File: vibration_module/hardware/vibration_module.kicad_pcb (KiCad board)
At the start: 2 copper layers, 19.8 x 18 mm, 17 parts, among them J1 I2C/PWR, SW2 SW_SPST, U2 DRV2605LDGS, U3 STM32G031G8Ux, U4 TPS7A20xxxDQN

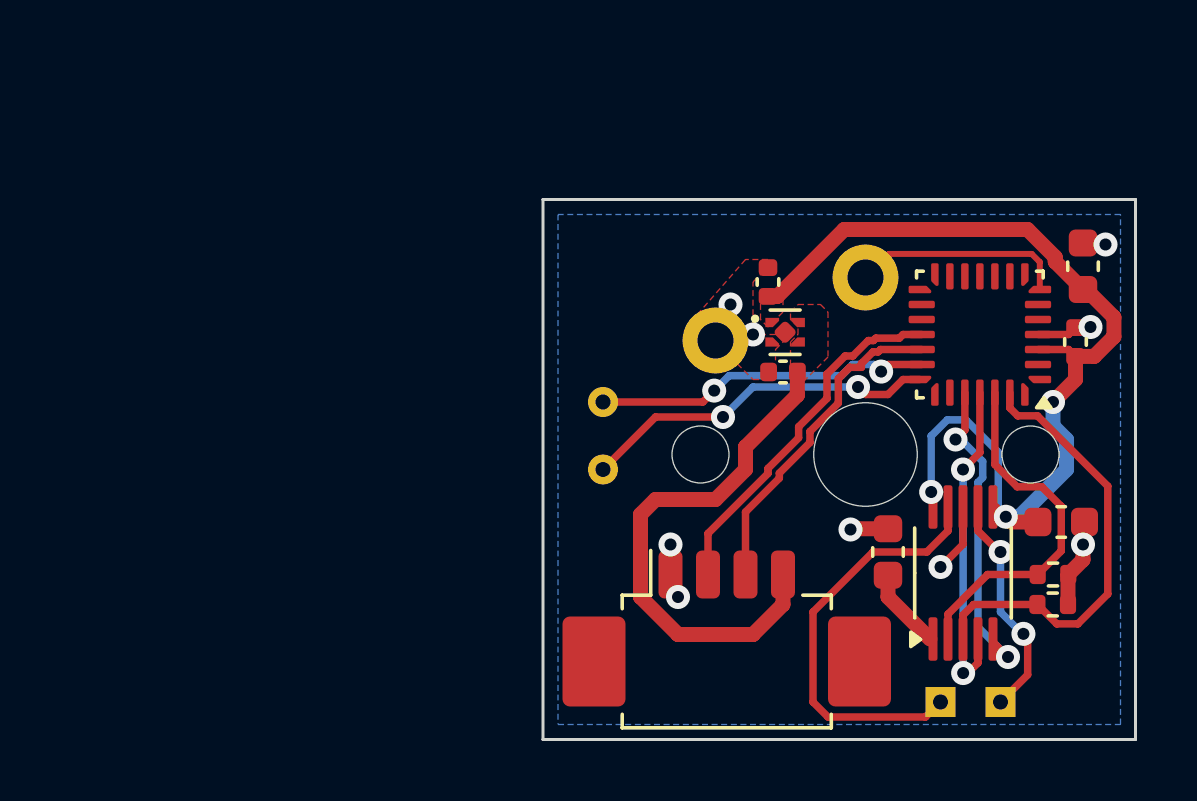
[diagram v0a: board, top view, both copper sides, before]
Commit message: update pcb layout, change switch bom
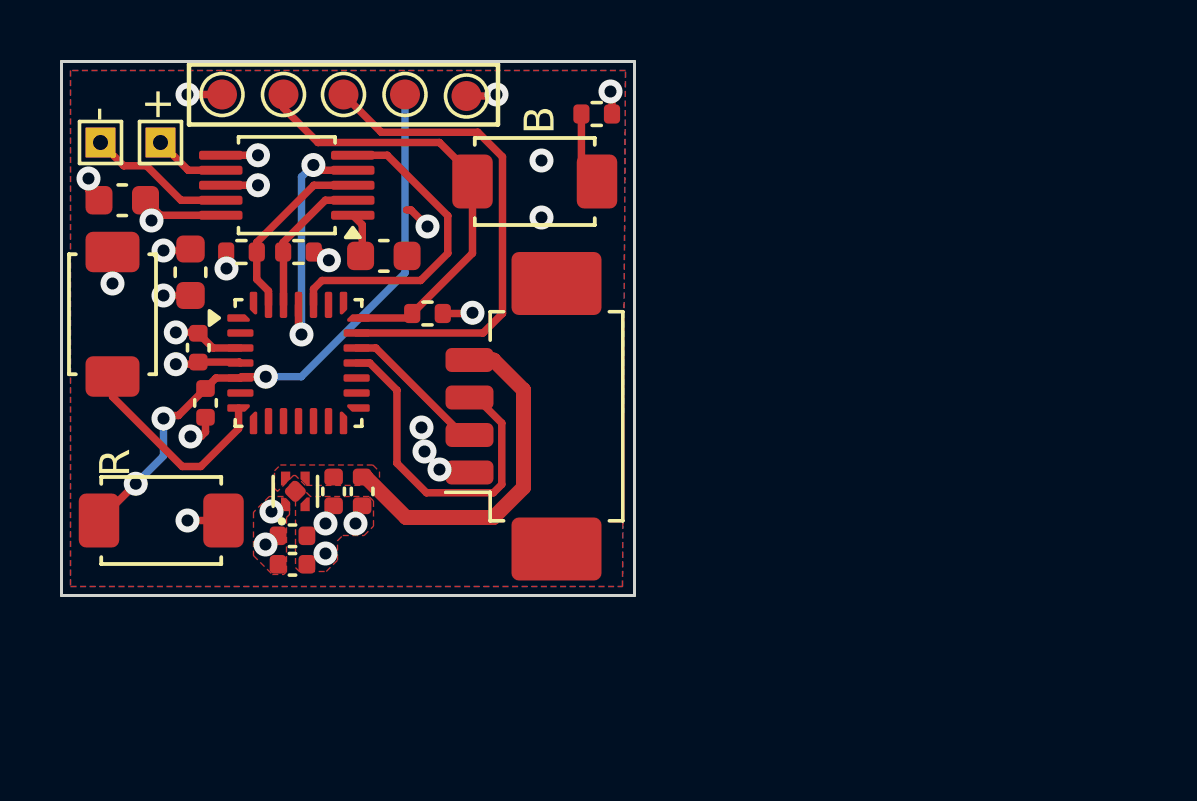
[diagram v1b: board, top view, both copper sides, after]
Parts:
- removed U4: TPS7A20xxxDQN, Package_SON:Texas_X2SON-4_1x1mm_P0.65mm
- added C3: 100n, Capacitor_SMD:C_0402_1005Metric, F.Cu at (162.3, 69.4)
- added C4: 100n, Capacitor_SMD:C_0402_1005Metric, F.Cu at (166.8, 74.2)
- added C5: 1u, Capacitor_SMD:C_0402_1005Metric, F.Cu at (167.7, 74.2)
- added R1: 330Ω, Resistor_SMD:R_0402_1005Metric, F.Cu at (175.5, 61.6)
- added R2: 10k, Resistor_SMD:R_0402_1005Metric, F.Cu at (169.9, 68.3)
- added SW1: NRST, PCM_JLCPCB:SW_TS-1088-AR02016, F.Cu at (161.0, 75.2)
- added SW3: SW_SPST, PCM_JLCPCB:SW_TS-1088-AR02016, F.Cu at (159.4, 68.3)
- added TP5: SWCLK, TestPoint:TestPoint_Pad_D1.0mm, F.Cu at (165.1, 61.0)
- added TP6: NRST, TestPoint:TestPoint_Pad_D1.0mm, F.Cu at (169.2, 61.0)
- added TP7: GND, TestPoint:TestPoint_Pad_D1.0mm, F.Cu at (171.2, 61.0)
- added U1: TPS7A20xxxDQN, Package_SON:Texas_X2SON-4_1x1mm_P0.65mm, F.Cu at (165.5, 74.2)
- C1: value 1u -> 100n; footprint Capacitor_SMD:C_0603_1608Metric -> Capacitor_SMD:C_0402_1005Metric
- C2: value 1u -> 10u
- C6: value 100n -> 1u
- C7: value 10u -> 100n; footprint Capacitor_SMD:C_0603_1608Metric -> Capacitor_SMD:C_0402_1005Metric
- C8, C9: footprint Capacitor_SMD:C_0402_1005Metric -> Capacitor_SMD:C_0603_1608Metric
- SW2: value SW_SPST -> BOOT0; footprint PCM_Switch_Keyboard_Kailh:SW_Kailh_Choc_V1_1.00u -> PCM_JLCPCB:SW_TS-1088-AR02016; moved to F.Cu
- TP1: value SWCLK -> M+; footprint TestPoint:TestPoint_THTPad_D1.0mm_Drill0.5mm -> TestPoint:TestPoint_THTPad_1.0x1.0mm_Drill0.5mm
- TP2: value SWDIO -> M-; footprint TestPoint:TestPoint_THTPad_D1.0mm_Drill0.5mm -> TestPoint:TestPoint_THTPad_1.0x1.0mm_Drill0.5mm
- TP3: value M+ -> 3V3; footprint TestPoint:TestPoint_THTPad_1.0x1.0mm_Drill0.5mm -> TestPoint:TestPoint_Pad_D1.0mm
- TP4: value M- -> SWDIO; footprint TestPoint:TestPoint_THTPad_1.0x1.0mm_Drill0.5mm -> TestPoint:TestPoint_Pad_D1.0mm
- U2: value DRV2605LDGS -> STM32G031G8Ux; footprint Package_SO:VSSOP-10_3x3mm_P0.5mm -> Package_DFN_QFN:QFN-28_4x4mm_P0.5mm
- U3: value STM32G031G8Ux -> DRV2605LDGS; footprint Package_DFN_QFN:QFN-28_4x4mm_P0.5mm -> Package_SO:VSSOP-10_3x3mm_P0.5mm
- moved TP3 31.4 mm to (163.1, 61.0)
- moved C2 30.2 mm to (162.0, 66.9), turned to 90 degrees
- moved TP4 29.8 mm to (167.1, 61.0)
- moved R3 29.5 mm to (163.7, 66.3), turned to 180 degrees
- moved C7 27.8 mm to (165.4, 75.7), turned to 180 degrees
- moved R4 27.4 mm to (165.6, 66.3)
- moved C6 27.1 mm to (165.4, 76.7), turned to 180 degrees
- moved U3 23.6 mm to (165.2, 64.0)
- moved C1 23.3 mm to (162.5, 71.3), turned to 90 degrees
- moved U2 23.2 mm to (165.6, 70.0), turned to 0 degrees
- moved C8 22.8 mm to (159.7, 64.5)
- moved TP2 18.9 mm to (159.0, 62.6), turned to 180 degrees
- moved TP1 18.3 mm to (161.0, 62.6), turned to 180 degrees
- moved SW2 14.3 mm to (173.5, 63.9), turned to 0 degrees
- moved C9 12.8 mm to (168.4, 66.4), turned to 180 degrees
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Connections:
- C1 pad 2: Net-(U2-REG) -> NRST
- C6 pad 1: +3.3V -> GND
- C6 pad 2: GND -> +3.3V
- C7 pad 1: +3.3V -> GND
- C7 pad 2: GND -> +3.3V
- C8 pad 1: VBUS -> +3.3V
- C9 pad 1: +3.3V -> GND
- C9 pad 2: GND -> Net-(U3-REG)
- J1 pad 2: /SCL -> I2C2_SDA
- J1 pad 3: /SDA -> I2C2_SCL
- R3 pad 1: Net-(U2-SDA) -> I2C1_SDA
- R3 pad 2: GND -> +3.3V
- R4 pad 1: Net-(U2-SCL) -> I2C1_SCL
- R4 pad 2: GND -> +3.3V
- SW2 pad 1: Net-(SW2-A) -> SWCLK/BOOT0
- SW2 pad 2: GND -> Net-(SW2-B)
- TP1 pad 1: Net-(U3-PA14) -> Net-(U3-OUT+)
- TP2 pad 1: Net-(U3-PA13) -> Net-(U3-OUT-)
- TP3 pad 1: Net-(U2-OUT-) -> +3.3V
- TP4 pad 1: Net-(U2-OUT+) -> SWDIO
- U2 pad 1: Net-(U2-REG) -> unconnected-(U2-PC14-Pad1)
- U2 pad 10: +3.3V -> unconnected-(U2-PA4-Pad10)
- U2 pad 2: Net-(U2-SCL) -> unconnected-(U2-PC15-Pad2)
- U2 pad 3: Net-(U2-SDA) -> +3.3V
- U2 pad 4: Net-(U2-IN/TRIG) -> GND
- U2 pad 5: Net-(U2-EN) -> NRST
- U2 pad 6: +3.3V -> unconnected-(U2-PA0-Pad6)
- U2 pad 7: Net-(U2-OUT+) -> SW
- U2 pad 8: GND -> unconnected-(U2-PA2-Pad8)
- U2 pad 9: Net-(U2-OUT-) -> unconnected-(U2-PA3-Pad9)
- U3 pad 1: unconnected-(U3-PC14-Pad1) -> Net-(U3-REG)
- U3 pad 10: unconnected-(U3-PA4-Pad10) -> +3.3V
- U3 pad 2: unconnected-(U3-PC15-Pad2) -> I2C1_SCL
- U3 pad 3: +3.3V -> I2C1_SDA
- U3 pad 4: GND -> IN/TRIG
- U3 pad 5: unconnected-(U3-PF2-Pad5) -> EN
- U3 pad 6: unconnected-(U3-PA0-Pad6) -> +3.3V
- U3 pad 7: Net-(SW2-A) -> Net-(U3-OUT+)
- U3 pad 8: unconnected-(U3-PA2-Pad8) -> GND
- U3 pad 9: unconnected-(U3-PA3-Pad9) -> Net-(U3-OUT-)
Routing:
- net +3.3V: track 33.5 -> 11.1 mm, vias 3 -> 10
- net NRST: track 0.00 -> 20.3 mm, vias 0 -> 3
- net SWDIO: track 0.00 -> 16.5 mm
- net SWCLK/BOOT0: track 0.00 -> 15.0 mm
- net Net-(U2-SDA): track 14.9 -> 0.00 mm
- net Net-(U2-OUT-): track 14.1 -> 0.00 mm
- net Net-(U2-SCL): track 12.2 -> 0.00 mm
- net /SCL: track 12.0 -> 0.00 mm
- net Net-(U3-PA14): track 12.0 -> 0.00 mm, vias 2 -> 0
- net I2C2_SCL: track 0.00 -> 11.6 mm
- net Net-(U3-PA13): track 11.3 -> 0.00 mm, vias 2 -> 0
- net /SDA: track 11.1 -> 0.00 mm
- net Net-(U2-IN/TRIG): track 11.0 -> 0.00 mm, vias 2 -> 0
- net EN: track 0.00 -> 10.8 mm
- net Net-(U2-EN): track 10.7 -> 0.00 mm, vias 2 -> 0
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- added copper zone on In2.Cu, net +3.3V
- added copper zone on In1.Cu, net GND
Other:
- board size 19.8 x 18 mm -> 19.1 x 17.8 mm
- copper layers 2 -> 4
- board text added: "+"
- board text added: "-"
- board text added: "B"
- board text added: "JLCJLCJLC"
- board text added: "OFBGlove Vibration Module gmmyung@kaist.ac.kr"
- board text added: "R"
